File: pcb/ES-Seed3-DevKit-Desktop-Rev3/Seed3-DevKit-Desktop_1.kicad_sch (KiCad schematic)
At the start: 80 parts, among them J7 USB4110GFA, U10 LD1117S50TR_SOT223, U12 CD4051B, U14 USBLC6-2SC6, U2 MCP6002-xSN, U4 CD4021BM96, U5 CD4021BM96, U6 MCP6002-xSN, U7 LMR62421XMF, U9 MCP6002-xSN

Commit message: schematic level changes for fixing CV idle offset, and audio whine tone.
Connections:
- net GND: now also J_CV_IN_1.NORM, J_CV_IN_2.NORM
- no-connect marks 15 -> 13
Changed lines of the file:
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@@
+	)
+	(junction
+		(at 335.28 200.66)
+		(diameter 0)
+		(color 0 0 0 0)
 	)
 	(junction
@@
 	(junction
 		(at 339.09 96.52)
+		(diameter 0)
+		(color 0 0 0 0)
+	)
+	(junction
+		(at 335.28 153.67)
 		(diameter 0)
 		(color 0 0 0 0)
@@
 	)
 	(no_connect
-		(at 331.47 198.12)
-	)
-	(no_connect
 		(at 260.35 248.92)
-	)
-	(no_connect
-		(at 331.47 151.13)
 	)
 	(no_connect
@@
 	(wire
 		(pts
+			(xy 335.28 198.12) (xy 335.28 200.66)
+		)
+		(stroke
+			(width 0)
+			(type default)
+		)
+	)
+	(wire
+		(pts
 			(xy 335.28 200.66) (xy 331.47 200.66)
 		)
@@
 	(wire
 		(pts
+			(xy 331.47 151.13) (xy 335.28 151.13)
+		)
+		(stroke
+			(width 0)
+			(type default)
+		)
+	)
+	(wire
+		(pts
 			(xy 312.42 63.5) (xy 306.07 63.5)
 		)
@@
 		(pts
 			(xy 363.22 148.59) (xy 365.76 148.59)
+		)
+		(stroke
+			(width 0)
+			(type default)
+		)
+	)
+	(wire
+		(pts
+			(xy 331.47 198.12) (xy 335.28 198.12)
 		)
 		(stroke
@@
 		)
 		(stroke
+			(width 0)
+			(type default)
+		)
+	)
+	(wire
+		(pts
+			(xy 335.28 151.13) (xy 335.28 153.67)
+		)
+		(stroke

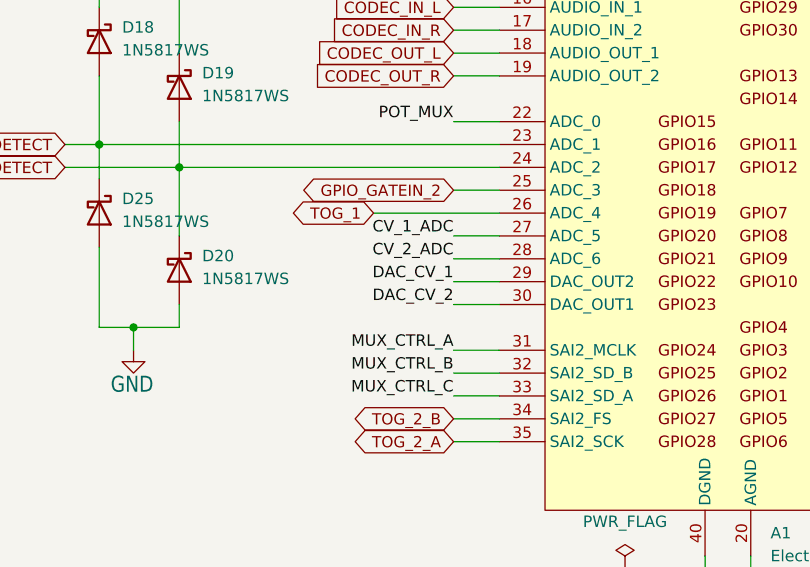
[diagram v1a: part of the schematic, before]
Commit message: updated changelog with rev3 changes, updated silkscreen for software pin mappings, and swapped DAC channels so the STM32 ch matches the names on the PCB.
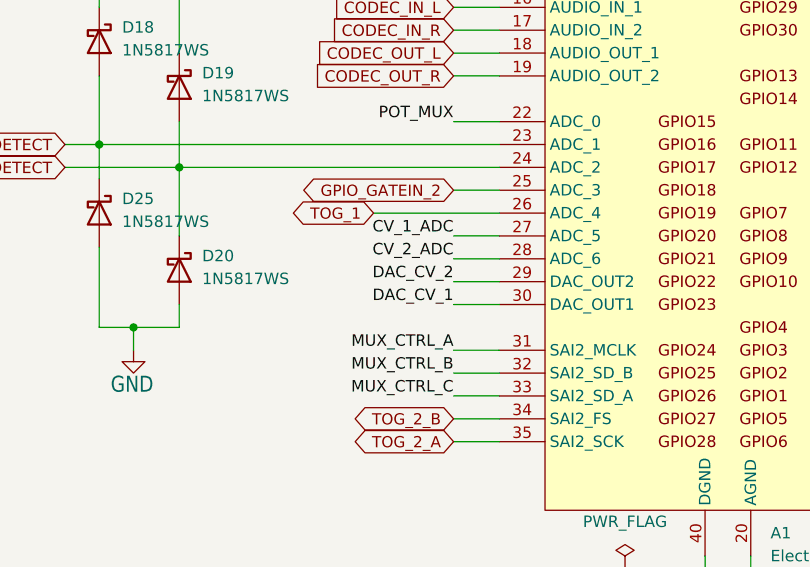
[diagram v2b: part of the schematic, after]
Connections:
- net DAC_CV_1: now also A1.30 (DAC_OUT1); no longer A1.29 (DAC_OUT2)
- net DAC_CV_2: now also A1.29 (DAC_OUT2); no longer A1.30 (DAC_OUT1)
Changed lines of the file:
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@@
 		)
 	)
-	(label "DAC_CV_2"
+	(label "DAC_CV_1"
 		(at 76.2 254 180)
 		(effects
@@
 		)
 	)
-	(label "DAC_CV_1"
+	(label "DAC_CV_2"
 		(at 76.2 251.46 180)
 		(effects

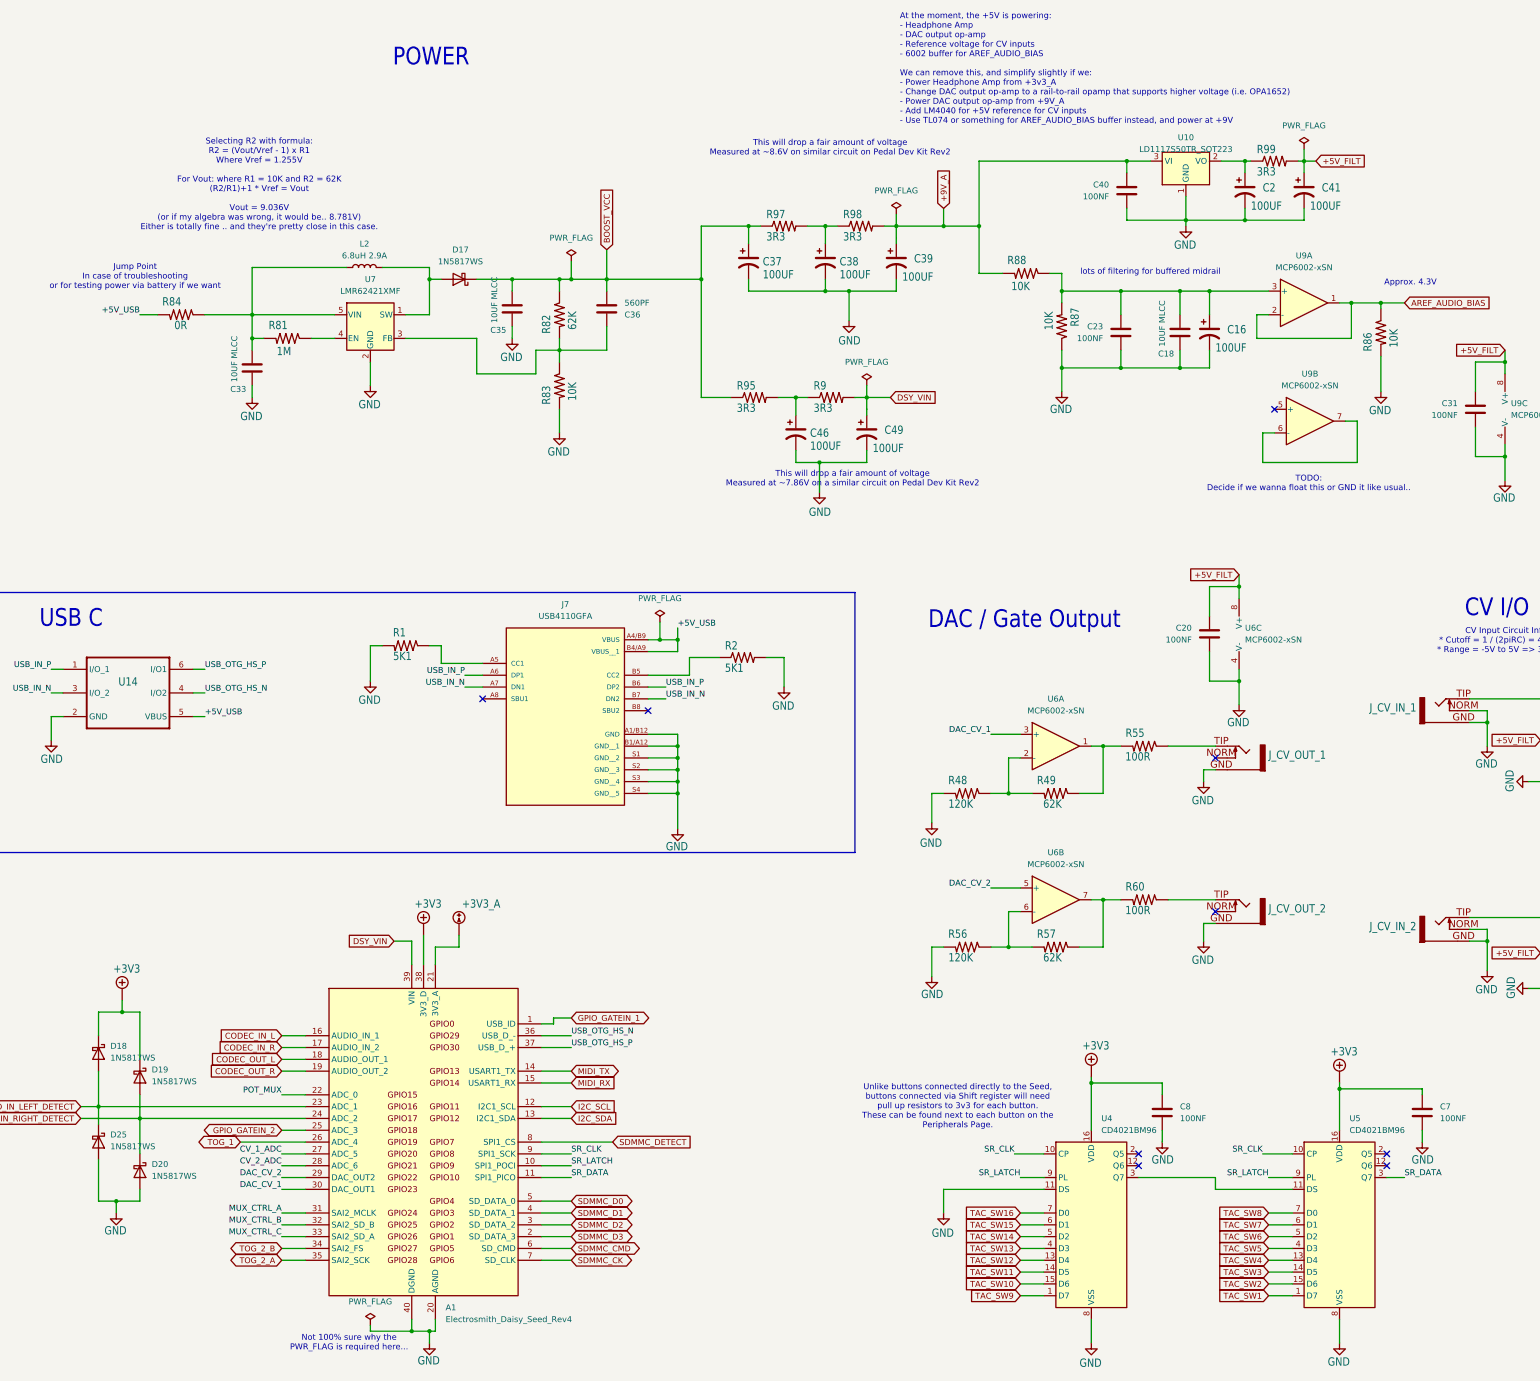
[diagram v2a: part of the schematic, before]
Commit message: partial directory update for cleanup of schematic comments after validating rev3 HW
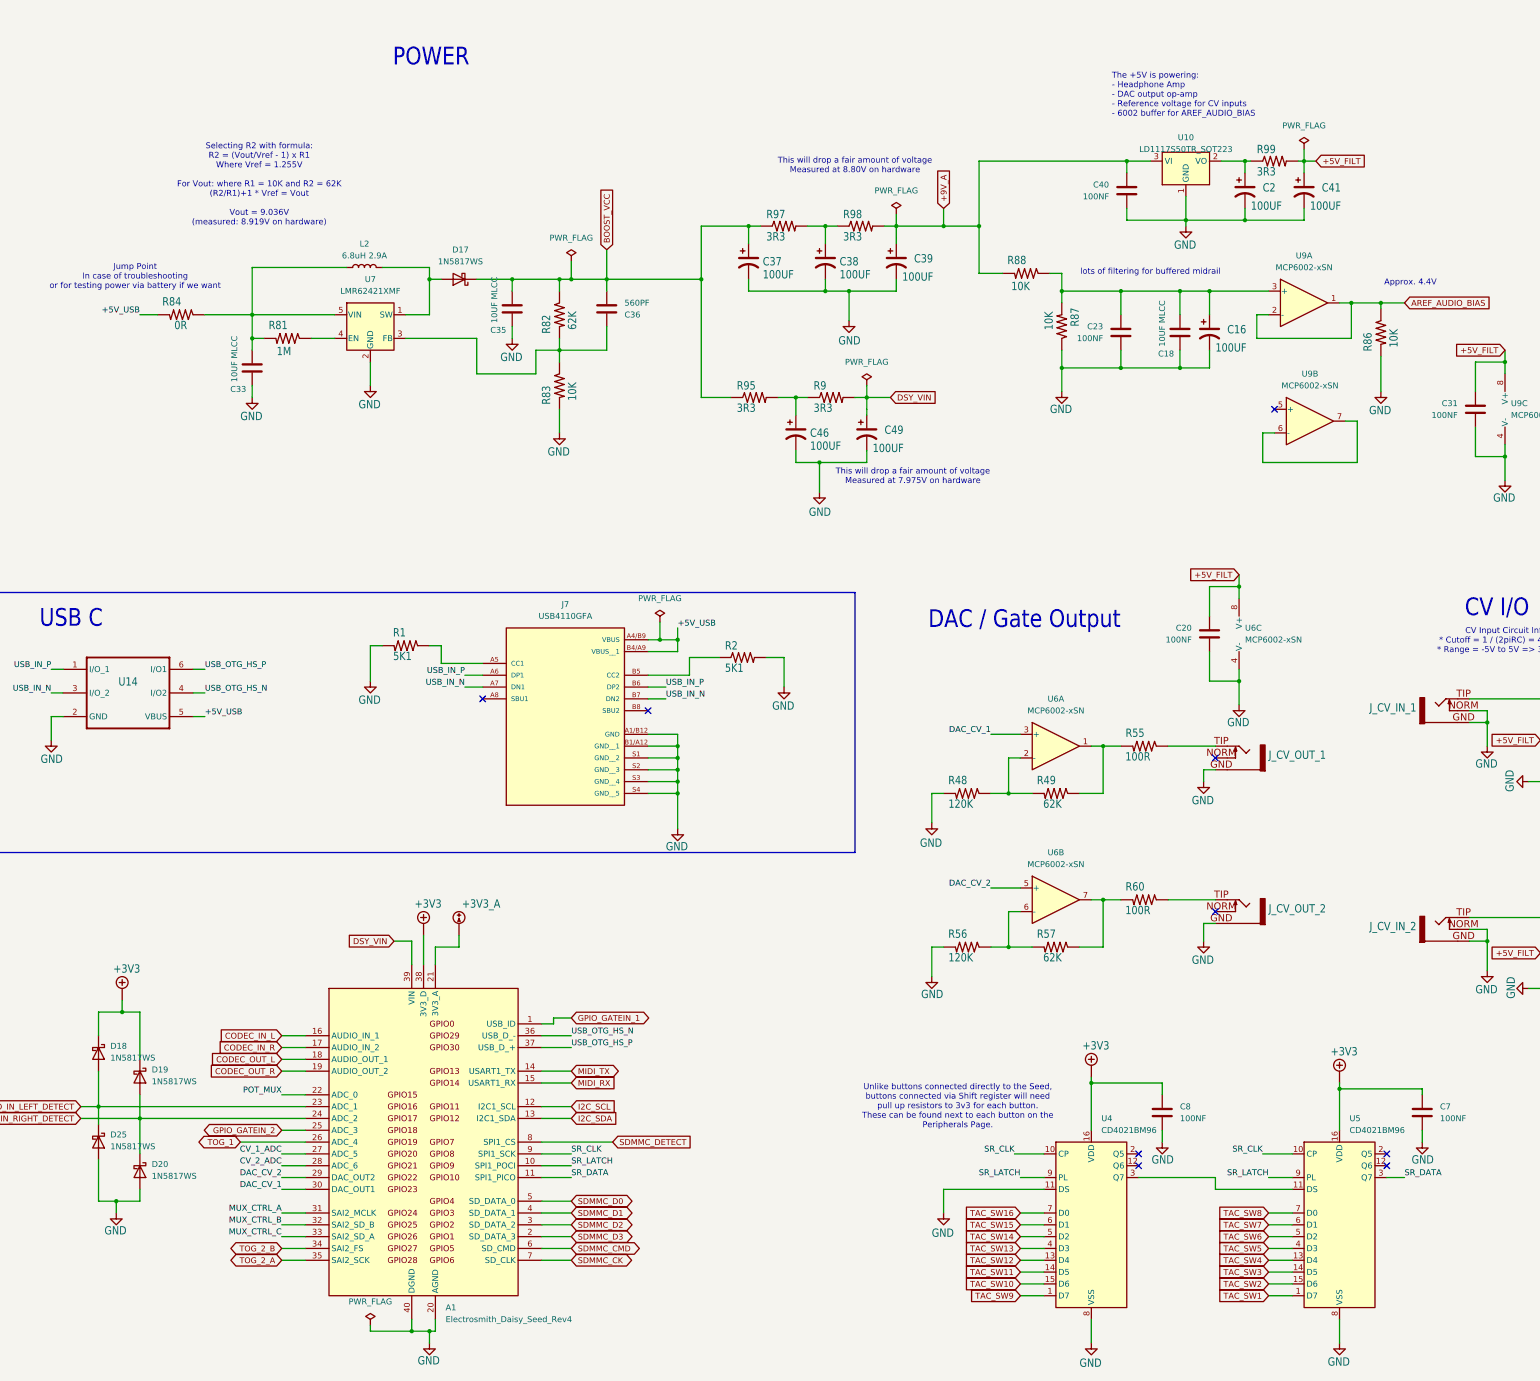
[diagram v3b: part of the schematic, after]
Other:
- note added: "Approx. 4.4V"
- note added: "Selecting R2 with formula: R2 = (Vout/Vref - 1) x R1 Where Vref = 1.255V For Vout: where R1 = 10K and R2 = 62K (R2/R1)+1 * Vref = Vout Vout = 9.036V (measured: 8.919V on hardware)"
- note added: "The +5V is powering: - Headphone Amp - DAC output op-amp - Reference voltage for CV inputs - 6002 buffer for AREF_AUDIO_BIAS"
- note added: "This will drop a fair amount of voltage Measured at 7.975V on hardware"
- note added: "This will drop a fair amount of voltage Measured at 8.80V on hardware"
- note removed: "Approx. 4.3V"
- note removed: "At the moment, the +5V is powering: - Headphone Amp - DAC output op-amp - Reference voltage for CV inputs - 6002 buffer for AREF_AUDIO_BIAS We can remove this, and simplify slightly if we: - Power Headphone Amp from +3v3_A - Change DAC output op-amp to a rail-to-rail opamp that supports higher voltage (i.e. OPA1652) - Power DAC output op-amp from +9V_A - Add LM4040 for +5V reference for CV inputs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"
- note removed: "Not 100% sure why the PWR_FLAG is required here..."
- note removed: "Selecting R2 with formula: R2 = (Vout/Vref - 1) x R1 Where Vref = 1.255V For Vout: where R1 = 10K and R2 = 62K (R2/R1)+1 * Vref = Vout Vout = 9.036V (or if my algebra was wrong, it would be.. 8.781V) Either is totally fine .. and they're pretty close in this case."
- note removed: "TODO: Decide if we wanna float this or GND it like usual.."
- note removed: "This will drop a fair amount of voltage Measured at ~7.86V on a similar circuit on Pedal Dev Kit Rev2"
- note removed: "This will drop a fair amount of voltage Measured at ~8.6V on similar circuit on Pedal Dev Kit Rev2"
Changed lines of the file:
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@@
 	(generator_version "9.0")
 	(paper "User" 425.45 298.602)
-	(text "This will drop a fair amount of voltage\nMeasured at ~7.86V on a similar circuit on Pedal Dev Kit Rev2"
+	(text "This will drop a fair amount of voltage\nMeasured at 7.975V on hardware"
 		(exclude_from_sim no)
-		(at 198.882 101.346 0)
+		(at 211.836 100.838 0)
 		(effects
 			(font
@@
 		)
 	)
-	(text "Selecting R2 with formula:\nR2 = (Vout/Vref - 1) x R1\nWhere Vref = 1.255V\n\nFor Vout: where R1 = 10K and R2 = 62K\n(R2/R1)+1 * Vref = Vout\n\nVout = 9.036V\n(or if my algebra was wrong, it would be.. 8.781V)\nEither is totally fine .. and they're pretty close in this case."
+	(text "Selecting R2 with formula:\nR2 = (Vout/Vref - 1) x R1\nWhere Vref = 1.255V\n\nFor Vout: where R1 = 10K and R2 = 62K\n(R2/R1)+1 * Vref = Vout\n\nVout = 9.036V\n(measured: 8.919V on hardware)"
 		(exclude_from_sim no)
 		(at 71.374 38.1 0)
@@
 		)
 	)
-	(text "Approx. 4.3V"
+	(text "Approx. 4.4V"
 		(exclude_from_sim no)
 		(at 318.77 59.182 0)
@@
 		)
 	)
-	(text "TODO:\nDecide if we wanna float this or GND it like usual.."
+	(text "The +5V is powering:\n- Headphone Amp\n- DAC output op-amp\n- Reference voltage for CV inputs\n- 6002 buffer for AREF_AUDIO_BIAS"
 		(exclude_from_sim no)
-		(at 296.926 102.362 0)
-		(effects
-			(font
-				(size 1.27 1.27)
-			)
-		)
-	)
-	(text "At the moment, the +5V is powering:\n- Headphone Amp\n- DAC output op-amp\n- Reference voltage for CV inputs\n- 6002 buffer for AREF_AUDIO_BIAS\n\nWe can remove this, and simplify slightly if we:\n- Power Headphone Amp from +3v3_A\n- Change DAC output op-amp to a rail-to-rail opamp that supports higher voltage (i.e. OPA1652)\n- Power DAC output op-amp from +9V_A\n- Add LM4040 for +5V reference for CV inputs\n- Use TL074 or something for AREF_AUDIO_BIAS buffer instead, and power at +9V"
-		(exclude_from_sim no)
-		(at 209.042 13.208 0)
+		(at 254.603 18.8397 0)
 		(effects
 			(font
@@
 		(exclude_from_sim no)
 		(at 221.488 236.22 0)
-		(effects
-			(font
-				(size 1.27 1.27)
-			)
-		)
-	)
-	(text "Not 100% sure why the \nPWR_FLAG is required here..."
-		(exclude_from_sim no)
-		(at 90.678 287.02 0)
 		(effects
 			(font
@@
 		)
 	)
-	(text "This will drop a fair amount of voltage\nMeasured at ~8.6V on similar circuit on Pedal Dev Kit Rev2"
+	(text "This will drop a fair amount of voltage\nMeasured at 8.80V on hardware"
 		(exclude_from_sim no)
-		(at 194.056 30.226 0)
+		(at 199.39 34.036 0)
 		(effects
 			(font
